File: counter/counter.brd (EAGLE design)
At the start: 124.1 x 30.3 mm, 57 parts, among them CON1 JACK_DC_BARREL, IC1 MCP1703DB, IC2 4067D, IC3 74HC154DW, J1 RJ12RIGHTANGLE-I2C, X2 8MHz, X4 MINI-USB

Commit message: counter
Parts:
- removed 12V: 12V, Headerlibrary:1X01
- removed 3V3: (no value), Headerlibrary:1X01
- removed C11: 100n, rcl:C0805
- removed C4: 10n, rcl:C0805
- removed CON1: JACK_DC_BARREL, lpatiny:DC_BARREL
- removed GND: GND, Headerlibrary:1X01
- removed R10: 1K, rcl:R0805
- removed RK1, RK2: 10K, resistor:M0805
- removed RT2: 4.7k, resistor:R0805
- removed SJ1: (no value), jumper:SJ
- removed U$1, U$3: QRE1113, SparkFun:QRE1113
- removed U$2: DS18B20, lpatiny:MSOP8
- added C14, C15, C18, C20, C21, C23, C25, C26, C28, C30, C32, C34, C5, C7, C8: 10n, rcl:C0805
- added I10, I12, I14, I16, I2, I4, I6, I8, O1, O11, O13, O15, O3, O5, O7, O9: QRE1113, SparkFun:QRE1113
- added RK10, RK12, RK14, RK18, RK20, RK22, RK24, RK26, RK28, RK30, RK32, RK34, RK36, RK38: 220, resistor:M0805
- added RK11, RK13, RK17, RK19, RK21, RK23, RK25, RK27, RK29, RK31, RK33, RK35, RK37, RK9: 1k, resistor:M0805
- moved J1 101.3 mm to (100.7, 20.4), turned to 180 degrees
- moved X2 99.6 mm to (91.8, 4.78), turned to 180 degrees
- moved CON_ISP 96.4 mm to (98.5, 5.71), turned to 0 degrees
- moved RK8 91.0 mm to (1.20, 21.6), flipped to the bottom, turned to 270 degrees
- moved RXT 85.3 mm to (70.5, 3.05), turned to 0 degrees
- moved RK5 79.8 mm to (5.24, 16.4), flipped to the bottom, turned to 270 degrees
- moved CX1 75.9 mm to (59.4, 2.30), turned to 0 degrees
- moved CU3 74.5 mm to (63.0, 6.00)
- moved BKLD 69.4 mm to (83.7, 3.56)
- moved R2 69.2 mm to (79.2, 3.56)
- moved IC3 68.0 mm to (53.0, 14.0)
- moved RK7 67.0 mm to (81.1, 7.28), turned to 209.2 degrees
- moved TX 66.4 mm to (64.1, 5.24), turned to 270 degrees
- moved C13 66.4 mm to (8.62, 4.96), turned to 180 degrees
- moved 32U4 66.3 mm to (72.3, 13.5)
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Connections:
- net N$12 renamed MUX2
- net N$6 renamed MUX1
- removed net N$11: IC3.2, U$3.2
- removed net N$9: R10.2, RT2.2, U$2.1
- new net DMUX1: IC3.1, O11.2
- new net DMUX10: IC3.10, O3.2
- new net DMUX11: IC3.11, O1.2
- new net DMUX12: I12.2, IC3.13
- new net DMUX13: IC3.14, O13.2
- new net DMUX14: I14.2, IC3.15
- new net DMUX15: IC3.16, O15.2
- new net DMUX16: I16.2, IC3.17
- new net DMUX2: I2.2, IC3.2
- new net DMUX3: I10.2, IC3.3
- new net DMUX4: I4.2, IC3.4
- new net DMUX5: IC3.5, O9.2
- new net DMUX6: I6.2, IC3.6
- new net DMUX7: IC3.7, O7.2
- new net DMUX8: I8.2, IC3.8
- new net DMUX9: IC3.9, O5.2
- new net MUX10: IC2.22, RK26.1
- new net MUX11: IC2.21, RK28.1
- new net MUX12: IC2.20, RK30.1
- new net MUX13: IC2.19, RK32.1
- new net MUX14: IC2.18, RK34.1
- new net MUX15: IC2.17, RK36.1
- new net MUX16: IC2.16, RK10.1
- new net MUX3: IC2.7, RK38.1
- new net MUX4: IC2.6, RK12.1
- new net MUX5: IC2.5, RK14.1
- new net MUX6: IC2.4, RK18.1
- new net MUX7: IC2.3, RK20.1
- new net MUX8: IC2.2, RK22.1
- new net MUX9: IC2.23, RK24.1
- new net N$14: C7.1, O3.3, RK10.2
- new net N$17: I4.1, RK11.2
- new net N$19: C8.1, I4.3, RK12.2
- new net N$21: O9.1, RK23.2
- new net N$22: O5.1, RK13.2
- new net N$23: C14.1, O5.3, RK14.2
- new net N$27: I6.1, RK17.2
- new net N$28: C15.1, I6.3, RK18.2
- new net N$31: C21.1, O9.3, RK24.2
- new net N$32: O7.1, RK19.2
- new net N$33: C18.1, O7.3, RK20.2
- new net N$35: I10.1, RK25.2
- new net N$36: C23.1, I10.3, RK26.2
- new net N$37: I8.1, RK21.2
- new net N$38: C20.1, I8.3, RK22.2
- new net N$39: O11.1, RK27.2
- new net N$41: C25.1, O11.3, RK28.2
- new net N$43: I12.1, RK29.2
- new net N$44: C26.1, I12.3, RK30.2
- new net N$45: O13.1, RK31.2
- new net N$46: C28.1, O13.3, RK32.2
- new net N$47: I14.1, RK33.2
- new net N$48: C30.1, I14.3, RK34.2
- new net N$49: O15.1, RK35.2
- new net N$50: C32.1, O15.3, RK36.2
- new net N$51: I16.1, RK37.2
- new net N$52: C34.1, I16.3, RK38.2
- net +12V: no longer 12V.1, CON1.P$1
- net 3.3V: now also C14.2, C15.2, C18.2, C20.2, C21.2, C23.2, C25.2, C26.2, C28.2, C30.2, C32.2, C34.2, C5.2, C7.2, C8.2, RK11.1, RK13.1, RK17.1, RK19.1, RK21.1, RK23.1, RK25.1, RK27.1, RK29.1, RK31.1, RK33.1, RK35.1, RK37.1, RK9.1; no longer 3V3.1, C4.2, RK1.1, RK2.1, RT2.1, U$2.8
- net D12*: now also IC2.15; no longer R10.1
- net GND: now also I10.4, I12.4, I14.4, I16.4, I2.4, I4.4, I6.4, I8.4, O1.4, O11.4, O13.4, O15.4, O3.4, O5.4, O7.4, O9.4; no longer C11.2, CON1.P$2, GND.1, SJ1.1, U$1.4, U$2.4, U$3.4
- net N$10: now also C5.1, I2.3; no longer C4.1, U$3.3
- net N$2: now also O3.1, RK9.2; no longer IC3.1, U$1.2
- net N$4: now also O1.1; no longer U$1.1
- net N$5: now also O1.3; no longer U$1.3
- net N$8: now also I2.1; no longer U$3.1
- net RESET: no longer C11.1, SJ1.2
- net SCL: no longer RK2.2
- net SDA: no longer RK1.2
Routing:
- net 3.3V: track 0.00 -> 104.3 mm, vias 0 -> 22
- net DMUX11: track 0.00 -> 71.0 mm, vias 0 -> 1
- net N$83: track 0.00 -> 27.0 mm
- net N$78: track 0.00 -> 27.0 mm
- net N$77: track 0.00 -> 27.0 mm
- net N$76: track 0.00 -> 27.0 mm
- net N$75: track 0.00 -> 27.0 mm
- net N$74: track 0.00 -> 27.0 mm
- net N$73: track 0.00 -> 27.0 mm
- net N$13: track 0.00 -> 27.0 mm
- net USB_N: track 0.00 -> 26.5 mm
- net USB_P: track 0.00 -> 26.5 mm
- net N$23: track 0.00 -> 13.6 mm
- net N$28: track 0.00 -> 13.6 mm
- net N$14: track 0.00 -> 13.4 mm
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- added copper zone on layer 1, net 3.3V
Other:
- board size 124.1 x 30.3 mm -> 109.2 x 25.9 mm
- board text removed: "12V"

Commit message: work in progress
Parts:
- moved C13 76.8 mm to (72.6, 47.4)
- moved CX2 69.4 mm to (63.7, 42.4)
- moved LDPW12 67.8 mm to (67.0, 47.4)
- moved RK6 58.5 mm to (59.1, 42.8)
- moved RK16 51.2 mm to (56.3, 43.3)
- moved RXLD 48.1 mm to (60.0, 39.4)
- moved R12 47.2 mm to (61.0, 35.4)
- moved RXT 36.2 mm to (63.9, 38.6)
- moved C10 32.4 mm to (27.7, 35.9)
- moved C12 27.5 mm to (16.1, 37.8)
- moved IC2 27.1 mm to (43.0, 37.6), turned to 270 degrees
- moved 32U4 24.1 mm to (75.4, 37.4)
- moved C2 18.9 mm to (6.13, 38.3)
- moved CU4 17.4 mm to (10.8, 36.4)
- moved IC3 11.8 mm to (43.2, 20.7), turned to 270 degrees
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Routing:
- net 3.3V: track 104.3 -> 13.3 mm, vias 22 -> 1
- net DMUX11: track 71.0 -> 7.52 mm
- net GND: track 0.00 -> 49.8 mm
- net USB_N: track 26.5 -> 0.00 mm
- net USB_P: track 26.5 -> 0.00 mm
- net N$23: track 13.6 -> 0.00 mm
- net N$28: track 13.6 -> 0.00 mm
- net N$14: track 13.4 -> 0.00 mm
- net N$33: track 13.0 -> 0.00 mm
- net N$10: track 10.7 -> 0.00 mm
- net N$36: track 10.5 -> 0.00 mm
- net N$52: track 9.10 -> 0.00 mm
- net N$38: track 8.84 -> 0.00 mm
- net N$41: track 8.42 -> 0.00 mm
- net N$44: track 8.23 -> 0.00 mm
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
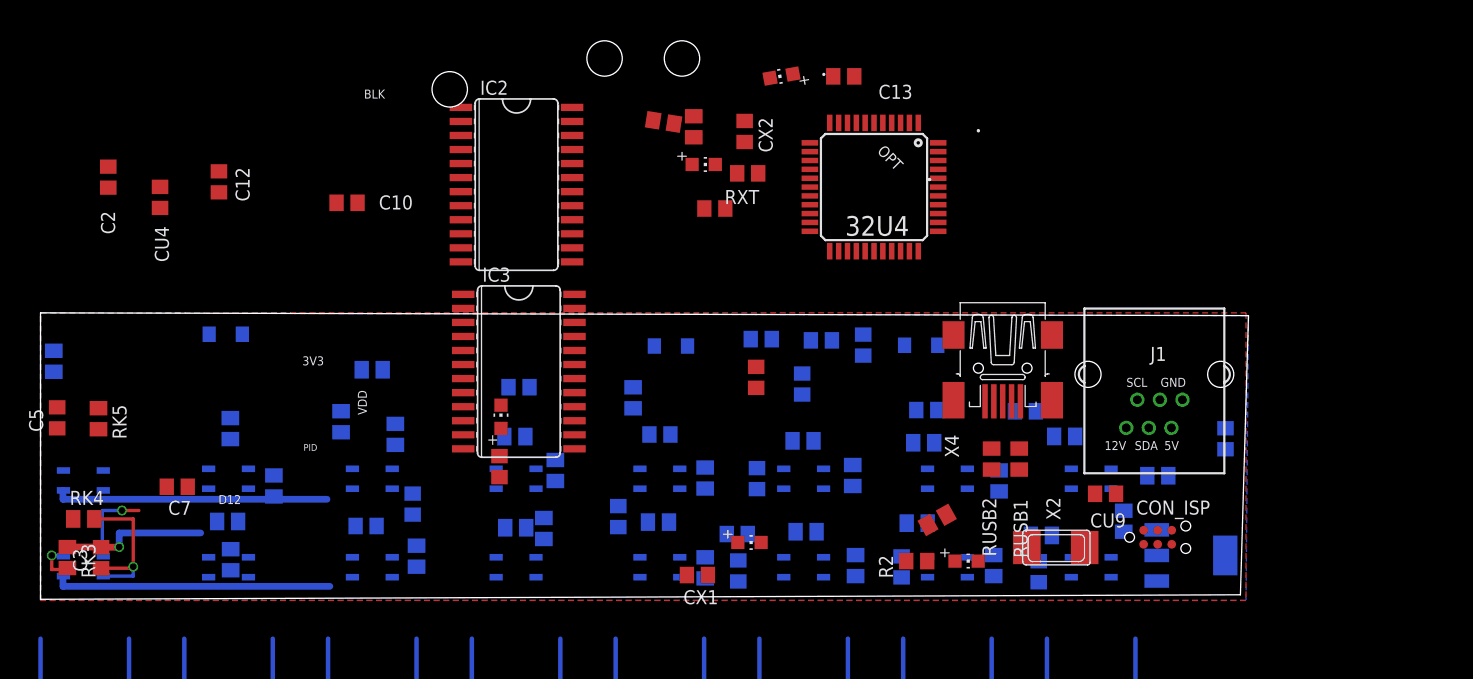
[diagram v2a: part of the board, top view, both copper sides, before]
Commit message: Places 16 IR LED emitter/receptors on board layout with defined distances, other parts can me moved to layout board.
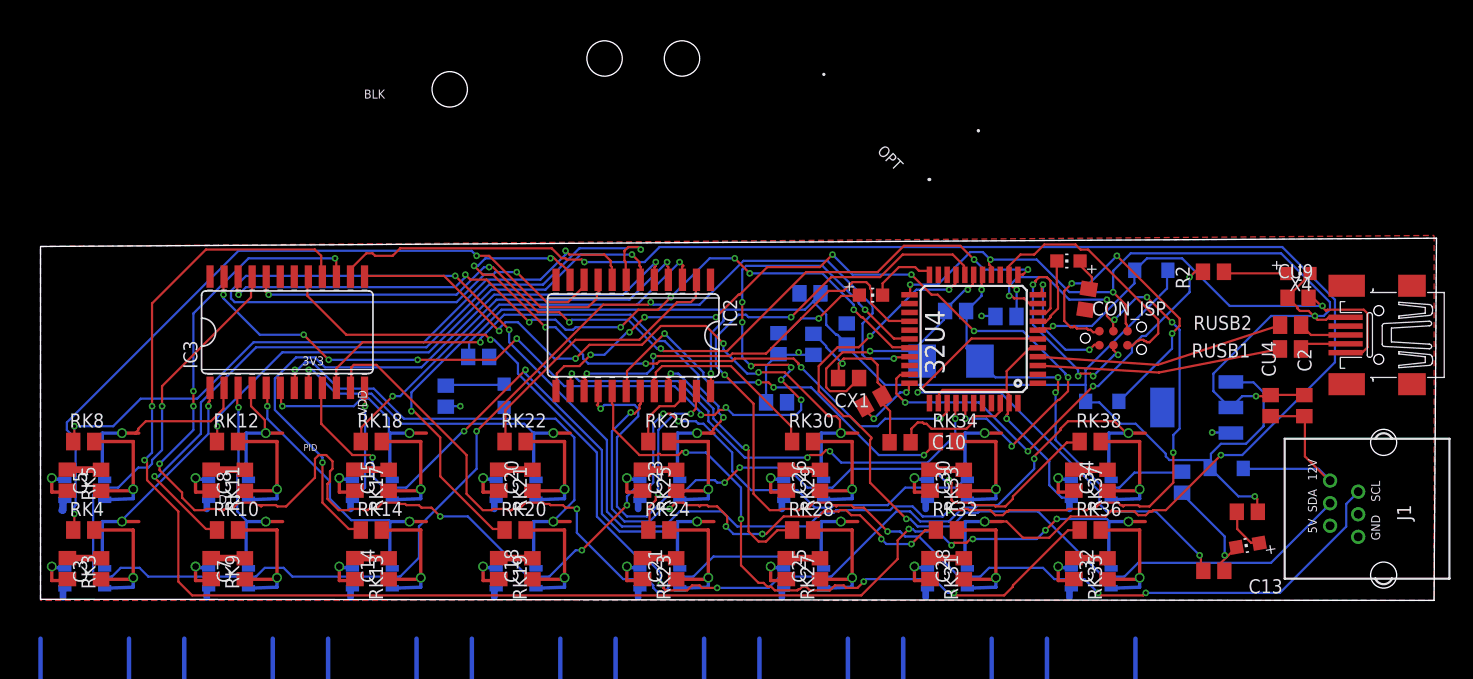
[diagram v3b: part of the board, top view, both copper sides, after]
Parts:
- moved C2 110.1 mm to (114.3, 17.6), turned to 90 degrees
- moved CU4 102.2 mm to (111.2, 17.6), turned to 90 degrees
- moved D1 91.3 mm to (107.2, 11.9), turned to 0 degrees
- moved C8 88.7 mm to (18.5, 10.9), flipped to the top, turned to 90 degrees
- moved LDPW12 59.8 mm to (109.2, 4.99)
- moved C13 55.8 mm to (106.1, 2.68)
- moved R12 55.4 mm to (109.1, 8.01)
- moved C10 54.5 mm to (77.7, 14.3)
- moved C12 54.2 mm to (66.5, 17.9), flipped to the bottom, turned to 0 degrees
- moved CX2 50.7 mm to (103.2, 10.7), flipped to the bottom, turned to 90 degrees
- moved RK16 41.5 mm to (94.6, 27.2), turned to 80.9 degrees
- moved BKLD 39.7 mm to (113.7, 29.6)
- moved D2 39.3 mm to (96.0, 18.0)
- moved C15 38.4 mm to (31.5, 10.9), flipped to the top
- moved R2 37.5 mm to (106.1, 29.7)
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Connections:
- net N$10 renamed Y2
- net N$14 renamed Y3
- net N$17 renamed RD4
- net N$19 renamed Y4
- net N$2 renamed RD3
- net N$21 renamed RD9
- net N$22 renamed RD5
- net N$23 renamed Y5
- net N$27 renamed RD6
- net N$28 renamed Y6
- net N$31 renamed Y9
- net N$32 renamed RD7
- net N$33 renamed Y7
- net N$35 renamed RD10
- net N$36 renamed Y10
- net N$37 renamed RD8
- net N$38 renamed Y8
- net N$39 renamed RD11
- net N$4 renamed RD1
- net N$41 renamed Y11
- net N$43 renamed RD12
- net N$44 renamed Y12
- net N$45 renamed RD13
- net N$46 renamed Y13
- net N$47 renamed RD14
- net N$48 renamed Y14
- net N$49 renamed RD15
- net N$5 renamed Y1
- net N$50 renamed Y15
- net N$51 renamed RD16
- net N$52 renamed Y16
- net N$8 renamed RD2
- removed net VCC: IC3.24
- removed net VSS: IC2.12
- net 3.3V: now also IC2.24, IC3.24
- net DMUX1: now also O1.2; no longer O11.2
- net DMUX10: now also I10.2; no longer O3.2
- net DMUX11: now also O11.2; no longer O1.2
- net DMUX3: now also O3.2; no longer I10.2
- net DMUX5: now also O5.2; no longer O9.2
- net DMUX9: now also O9.2; no longer O5.2
- net GND: now also IC2.12
- net MUX16: now also RK38.1; no longer RK10.1
- net MUX3: now also RK10.1; no longer RK38.1
- net VDD: no longer IC2.24
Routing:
- net MOSI: track 0.00 -> 179.6 mm, vias 0 -> 10
- net DMUX13: track 0.00 -> 144.7 mm, vias 0 -> 3
- net DMUX15: track 0.00 -> 143.7 mm, vias 0 -> 8
- net DMUX14: track 0.00 -> 141.1 mm, vias 0 -> 10
- net D10*: track 0.00 -> 132.7 mm, vias 0 -> 4
- net VDD: track 0.00 -> 120.0 mm, vias 0 -> 2
- net GND: track 49.8 -> 167.7 mm, vias 0 -> 9
- net DMUX16: track 0.00 -> 107.8 mm, vias 0 -> 5
- net SCL: track 0.00 -> 107.5 mm, vias 0 -> 5
- net D8*: track 0.00 -> 96.9 mm, vias 0 -> 14
- net D11*: track 0.00 -> 80.8 mm, vias 0 -> 6
- net SDA: track 0.00 -> 78.1 mm, vias 0 -> 3
- net A2: track 0.00 -> 72.1 mm, vias 0 -> 10
- net D9*: track 0.00 -> 71.8 mm, vias 0 -> 8
- net MUX1: track 0.00 -> 68.8 mm, vias 0 -> 2
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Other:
- board size 109.2 x 25.9 mm -> 126.2 x 32.8 mm

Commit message: clean up
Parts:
- removed C1, C2: 100n, rcl:C0805
- removed C23, C26, C28, C3, C30, C32, C34: 10n, rcl:C0805
- removed CU3, CU4: 10u, rcl:C0805
- removed I10, I12, I14, I16, I2, I4, I6, I8, O1: QRE1113, SparkFun:QRE1113
- removed LDPW12: RED, adafruit:CHIP-LED0805
- removed R12: 10k, rcl:R0805
- removed RK15, RK16: 1k, rcl:R0805
- removed RK3, RK37: 1k, resistor:M0805
- removed RK38, RK4: 220, resistor:M0805
- removed RXLD: RX, adafruit:CHIP-LED0805
- removed TX: TX, adafruit:CHIP-LED0805
- added C11, C16, C17, C19, C24, C6, C9: 10n, rcl:C0805
- added O10, O12, O14, O16, O19, O20, O4, O6, O8: QRE1113, SparkFun:QRE1113
- added RK41, RK43: 1k, resistor:M0805
- added RK42, RK44: 220, resistor:M0805
- R14, R2: value 1k -> 10k
- moved R14 61.3 mm to (96.6, 30.9), flipped to the top, turned to 180 degrees
- moved LDPW3 52.1 mm to (92.5, 30.9), flipped to the top, turned to 90 degrees
- moved CU8 41.9 mm to (106.0, 2.03), flipped to the top, turned to 0 degrees
- moved C13 41.7 mm to (67.2, 17.7), turned to 270 degrees
- moved O13 40.9 mm to (42.5, 12.7)
- moved RK32 40.7 mm to (41.3, 3.81), turned to 90 degrees
- moved RK26 40.6 mm to (96.5, 12.7), turned to 270 degrees
- moved RK25 39.6 mm to (94.0, 12.7), turned to 90 degrees
- moved RK31 36.6 mm to (43.8, 3.81)
- moved CU7 35.3 mm to (106.2, 12.4), flipped to the top, turned to 0 degrees
- moved RK27 29.1 mm to (96.5, 3.81)
- moved O9 28.8 mm to (29.2, 12.7)
- moved IC3 28.6 mm to (50.9, 24.4), turned to 270 degrees
- moved O11 28.3 mm to (95.2, 12.7)
- moved RK24 28.1 mm to (27.9, 3.81), turned to 90 degrees
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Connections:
- removed net +12V: C2.1, CU4.1, D1.A, J1.+12V
- removed net 5: J1.+5V
- removed net N$18: RK15.2, TX.A
- removed net N$24: RK16.2, RXLD.A
- removed net N$7: LDPW12.A, R12.1
- removed net RD1: O1.1, RK3.2
- removed net RD2: I2.1, RK5.2
- removed net Y1: C3.1, O1.3, RK4.2
- removed net Y2: C5.1, I2.3, RK8.2
- new net 1: J1.+12V
- new net 5VI2C: D1.A, J1.+5V
- new net RD19: O19.1, RK41.2
- new net RD20: O20.1, RK43.2
- new net Y19: C24.1, O19.3, RK42.2
- new net Y20: C25.1, O20.3, RK44.2
- net 3.3V: now also C11.2, C16.2, C17.2, C19.2, C24.2, C6.2, C9.2, RK41.1, RK43.1; no longer C23.2, C26.2, C28.2, C3.2, C30.2, C32.2, C34.2, RK15.1, RK16.1, RK3.1, RK37.1
- net A0: now also IC3.23; no longer IC2.11
- net A1: now also IC3.22; no longer IC2.14
- net A2: now also IC3.21; no longer IC2.13
- net A3: now also IC3.20
- net A4: now also IC2.1
- net A6: now also J1.GND2
- net D10*: now also IC2.15; no longer IC3.21
- net D11*: no longer IC3.20
- net D12*: no longer IC2.15
- net D5*: now also IC2.10
- net D6*: now also IC2.13
- net D8*: now also IC2.14; no longer IC3.23
- net D9*: now also IC2.11; no longer IC3.22
- net DMUX1: now also IC3.2, O3.2; no longer IC3.1, O1.2
- net DMUX10: now also O8.2; no longer I10.2
- net DMUX11: now also IC3.17, O15.2; no longer IC3.11, O11.2
- net DMUX12: now also IC3.11, O16.2; no longer I12.2, IC3.13
- net DMUX13: now also IC3.16, O19.2; no longer IC3.14, O13.2
- net DMUX14: now also IC3.13, O20.2; no longer I14.2, IC3.15
- net DMUX15: now also IC3.15, O11.2; no longer IC3.16, O15.2
- net DMUX16: now also IC3.14, O12.2; no longer I16.2, IC3.17
- net DMUX2: now also IC3.1, O4.2; no longer I2.2, IC3.2
- net DMUX3: now also IC3.8, O5.2; no longer IC3.3, O3.2
- net DMUX4: now also IC3.3, O6.2; no longer I4.2, IC3.4
- net DMUX5: now also IC3.7, O9.2; no longer IC3.5, O5.2
- net DMUX6: now also IC3.4, O10.2; no longer I6.2, IC3.6
- net DMUX7: now also IC3.6, O13.2; no longer IC3.7, O7.2
- net DMUX8: now also IC3.5, O14.2; no longer I8.2, IC3.8
- net DMUX9: now also O7.2; no longer O9.2
- net GND: now also IC3.18, IC3.19, O10.4, O12.4, O14.4, O16.4, O19.4, O20.4, O4.4, O6.4, O8.4; no longer C1.2, C2.2, CU3.2, CU4.2, I10.4, I12.4, I14.4, I16.4, I2.4, I4.4, I6.4, I8.4, J1.GND2, LDPW12.C, O1.4
- net MOSI: no longer IC2.10
- net MUX1: now also IC2.3, RK8.1; no longer IC2.9, RK4.1
- net MUX10: now also RK20.1; no longer RK26.1
- net MUX11: now also IC2.17, RK34.1; no longer IC2.21, RK28.1
- net MUX12: now also IC2.16, RK36.1; no longer IC2.20, RK30.1
- net MUX13: now also RK42.1; no longer RK32.1
- net MUX14: now also RK44.1; no longer RK34.1
- net MUX15: now also IC2.21, RK26.1; no longer IC2.17, RK36.1
- net MUX16: now also IC2.20, RK28.1; no longer IC2.16, RK38.1
- net MUX2: now also IC2.2, RK10.1; no longer IC2.8, RK8.1
- net MUX3: now also IC2.9, RK12.1; no longer IC2.7, RK10.1
- net MUX4: now also IC2.4, RK14.1; no longer IC2.6, RK12.1
- net MUX5: now also IC2.8, RK22.1; no longer IC2.5, RK14.1
- net MUX6: now also IC2.5, RK24.1; no longer IC2.4, RK18.1
- net MUX7: now also IC2.7, RK30.1; no longer IC2.3, RK20.1
- net MUX8: now also IC2.6, RK32.1; no longer IC2.2, RK22.1
- net MUX9: now also RK18.1; no longer RK24.1
- net RD10: now also O10.1, RK23.2; no longer I10.1, RK25.2
- net RD11: now also RK25.2; no longer RK27.2
- net RD12: now also O12.1, RK27.2; no longer I12.1, RK29.2
- net RD13: now also RK29.2; no longer RK31.2
- net RD14: now also O14.1, RK31.2; no longer I14.1, RK33.2
- net RD15: now also RK33.2; no longer RK35.2
- net RD16: now also O16.1, RK35.2; no longer I16.1, RK37.2
- net RD3: now also RK5.2; no longer RK9.2
- net RD4: now also O4.1, RK9.2; no longer I4.1, RK11.2
- net RD5: now also RK11.2; no longer RK13.2
- net RD6: now also O6.1, RK13.2; no longer I6.1, RK17.2
- net RD7: now also RK17.2; no longer RK19.2
- net RD8: now also O8.1, RK19.2; no longer I8.1, RK21.2
- net RD9: now also RK21.2; no longer RK23.2
- net RXLED: no longer RXLD.C
- net TXLED: no longer TX.C
- net VDD: no longer C1.1, CU3.1, R12.2
- net Y10: now also C15.1, O10.3, RK24.2; no longer C23.1, I10.3, RK26.2
- net Y11: now also C16.1, RK26.2; no longer C25.1, RK28.2
- net Y12: now also C17.1, O12.3, RK28.2; no longer C26.1, I12.3, RK30.2
- net Y13: now also C18.1, RK30.2; no longer C28.1, RK32.2
- net Y14: now also C19.1, O14.3, RK32.2; no longer C30.1, I14.3, RK34.2
- net Y15: now also C20.1, RK34.2; no longer C32.1, RK36.2
- net Y16: now also C21.1, O16.3, RK36.2; no longer C34.1, I16.3, RK38.2
- net Y3: now also C5.1, RK8.2; no longer C7.1, RK10.2
- net Y4: now also C6.1, O4.3, RK10.2; no longer C8.1, I4.3, RK12.2
- net Y5: now also C7.1, RK12.2; no longer C14.1, RK14.2
- net Y6: now also C8.1, O6.3, RK14.2; no longer C15.1, I6.3, RK18.2
- net Y7: now also C9.1, RK18.2; no longer C18.1, RK20.2
- net Y8: now also C11.1, O8.3, RK20.2; no longer C20.1, I8.3, RK22.2
- net Y9: now also C14.1, RK22.2; no longer C21.1, RK24.2
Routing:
- net 3.3V: track 61.5 -> 379.2 mm, vias 4 -> 2
- net GND: track 167.7 -> 391.6 mm, vias 9 -> 33
- net MOSI: track 179.6 -> 39.1 mm, vias 10 -> 2
- net VDD: track 120.0 -> 13.7 mm, vias 2 -> 0
- net DMUX14: track 141.1 -> 40.0 mm, vias 10 -> 3
- net DMUX13: track 144.7 -> 50.5 mm, vias 3 -> 1
- net DMUX15: track 143.7 -> 61.6 mm, vias 8 -> 1
- net D11*: track 80.8 -> 0.00 mm, vias 6 -> 0
- net D10*: track 132.7 -> 52.2 mm, vias 4 -> 2
- net A4: track 0.00 -> 69.5 mm, vias 0 -> 2
- net A6: track 0.00 -> 68.2 mm, vias 0 -> 1
- net DMUX7: track 46.1 -> 112.9 mm, vias 2 -> 3
- net DMUX8: track 32.0 -> 95.5 mm, vias 2 -> 1
- net D5*: track 0.00 -> 61.9 mm, vias 0 -> 2
- net DMUX6: track 21.4 -> 83.0 mm, vias 2 -> 1
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- removed copper zone on layer 1, net 3.3V
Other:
- board size 126.2 x 32.8 mm -> 126.2 x 32 mm
- board text removed: "BLK"
- board text removed: "C:/Users/G/Pictures/logo_epfl.bmp"
- board text removed: "D11"
- board text removed: "Hive 1.0"
- board text removed: "IF LoRa"
- board text removed: "LoRa RN2483"
- board text removed: "MEM SELECT"
- board text removed: "OPT"
- board text removed: "Rx"
- board text removed: "SPI"
